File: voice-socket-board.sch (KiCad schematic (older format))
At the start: 290 parts, among them J1 JACK_MONO_SW, J2 JACK_MONO_SW, J3 JACK_MONO_SW, P1 CONN_01X03, P2 CONN_01X03, P3 CONN_02X05, P4 DDR3-DIMM, Q1 MMBT3904, Q10 2N3906, Q2 DMMT3904W, Q3 2N7002, Q4 2N7002, Q5 MMBT3904, Q6 2N3906, Q7 MMBT3904, Q8 MMBT3904, Q9 MMBT3904, SW1 SPST, SW10 SP3T, SW11 SP3T, SW12 SP3T, SW13 SP3T, SW14 SPST, SW15 TACT_SWITCH, SW2 SPST, SW3 SP3T, SW4 SP3T, SW5 SPST, SW6 SPST, SW7 Switch_SPDT_x2, SW8 2P3T, SW9 SP3T, U1 LM833, U10 TL072-, U11 NE5534, U2 TL072-, U3 TL072-, U4 TL072-, U5 TL072-, U6 TL072-, U7 MAX9945, U8 CD4013, U9 TL072-

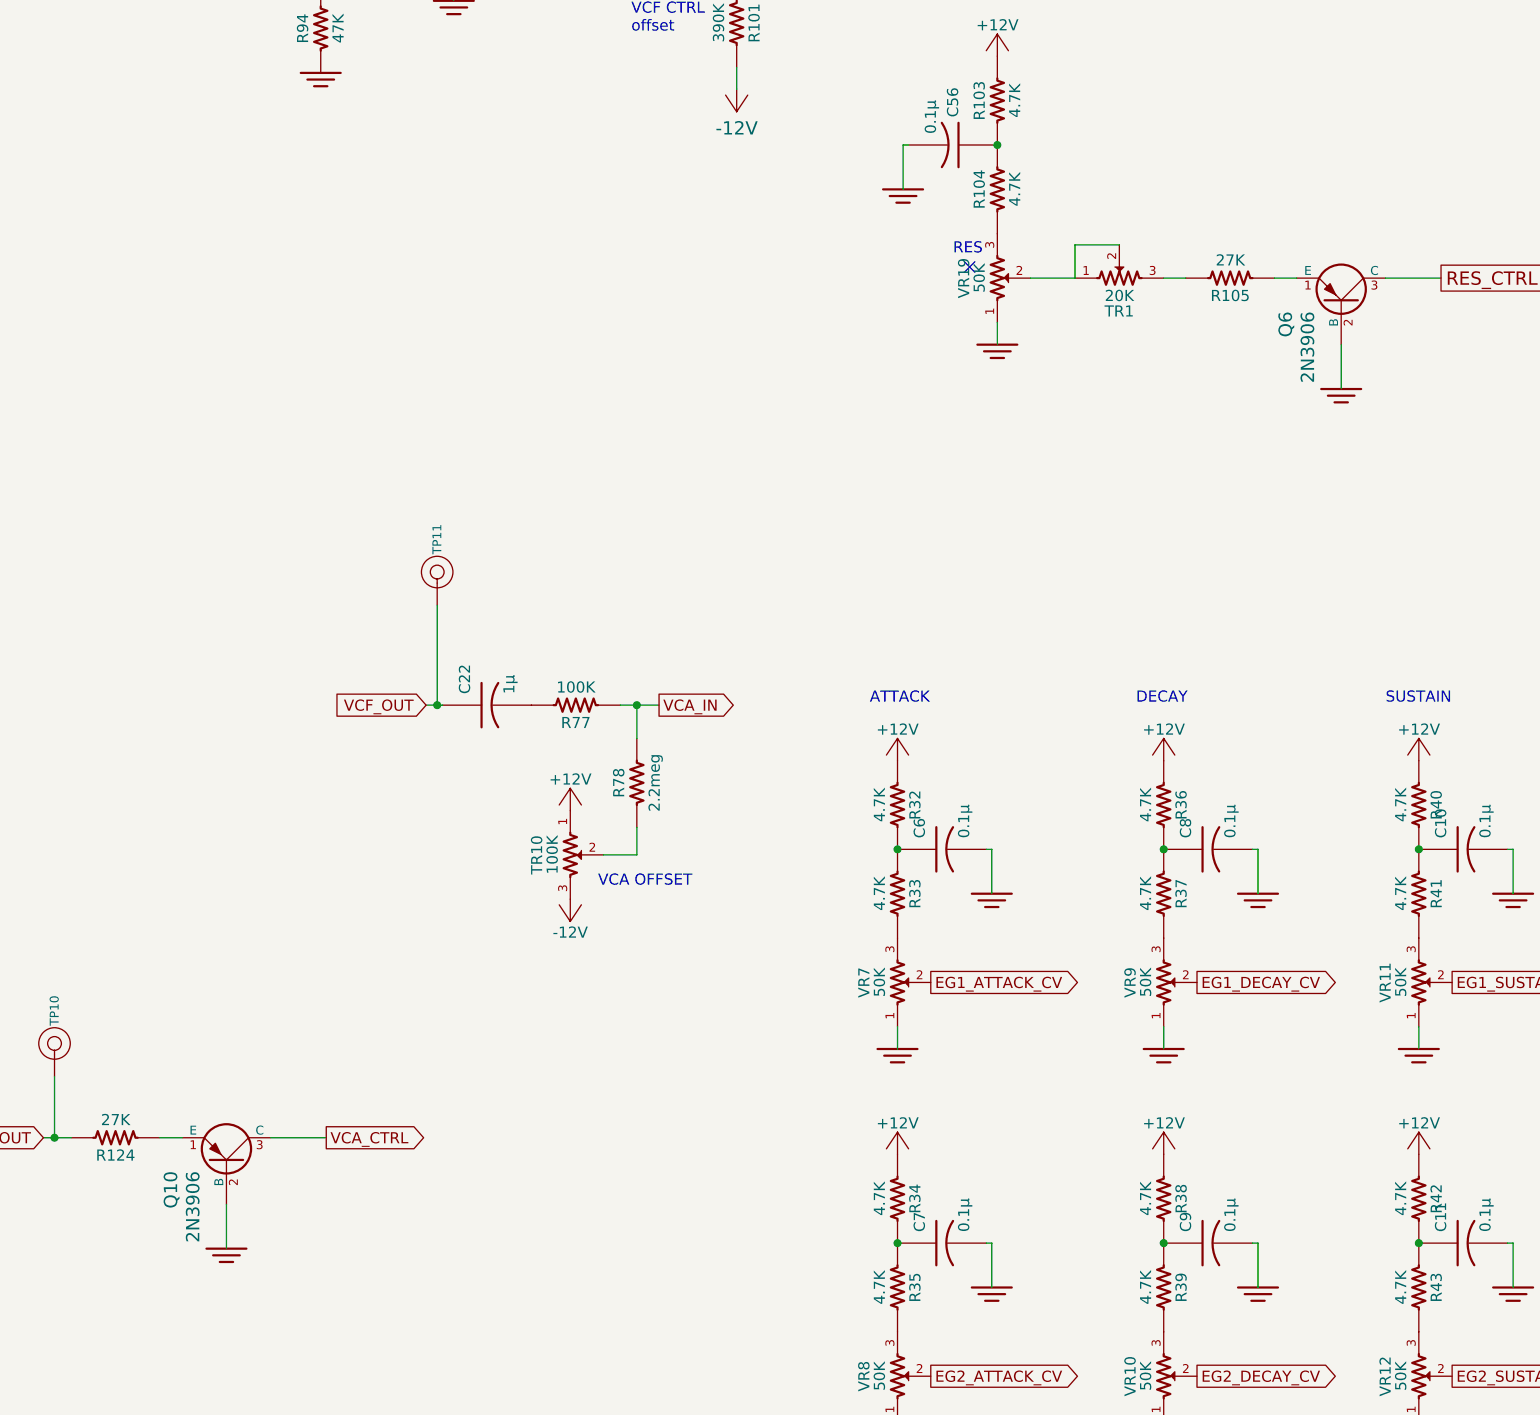
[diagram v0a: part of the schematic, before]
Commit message: changing out all SOT23 footprints for SOT23-132 - pin numbering was previously inconsistent and incoorect for LM4040 and MMBT3904 symbols and footprints
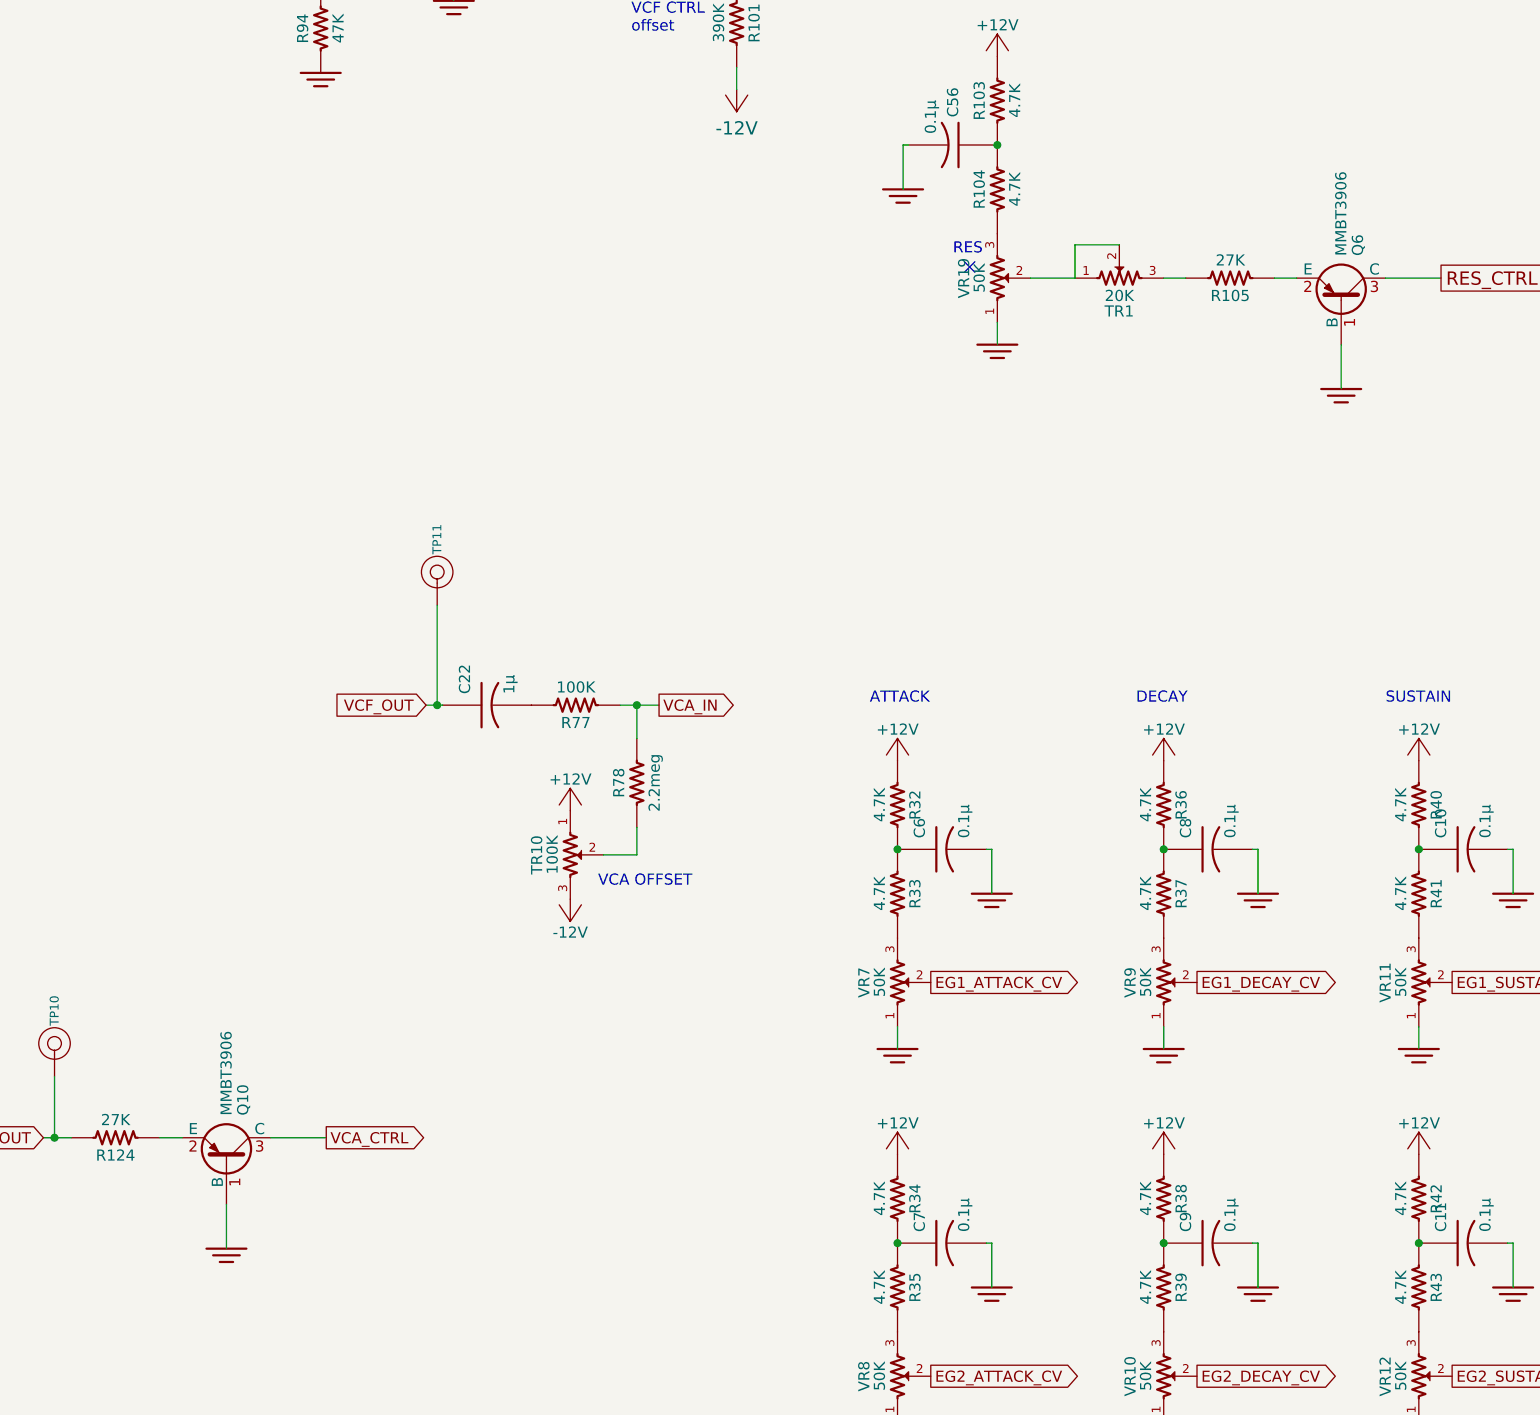
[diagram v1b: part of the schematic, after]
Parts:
- removed Q10, Q6: 2N3906, MyModules:SOT23-JRL, symbol PNP
- added Q10, Q6: MMBT3906, MyModules:SOT23-132-JRL, symbol MMBT3906
- D10, D11: footprint MyModules:SMB -> MyModules:SMB-1C2A
- Q1, Q5, Q7, Q8, Q9: footprint MyModules:SOT23-JRL -> MyModules:SOT23-132-JRL
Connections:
- net GND: now also Q10.1 (B), Q6.1 (B)
- net RES_CTRL: now also Q6.3 (C)
- net VCA_CTRL: now also Q10.3 (C)
- net at R105.1: now also Q6.2 (E)
- net at R124.1: now also Q10.2 (E)
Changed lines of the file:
@@
 $EndComp
 $Comp
-L PNP Q6
-U 1 1 5664F02B
-P 22300 25625
-F 0 "Q6" H 22250 25375 60  0000 R CNN
-F 1 "2N3906" H 22250 25475 60  0000 R CNN
-F 2 "MyModules:SOT23-JRL" H 22300 25625 60  0001 C CNN
-F 3 "~" H 22300 25625 60  0000 C CNN
-	1    22300 25625
-	0    1    -1   0
-$EndComp
-$Comp
 L POT_US TR1
 U 1 1 5664F02C
@@
 F 0 "Q7" H 11200 26125 50  0000 L CNN
 F 1 "MMBT3904" H 11200 26050 50  0000 L CNN
-F 2 "MyModules:SOT23-JRL" H 11200 25975 50  0001 L CIN
+F 2 "MyModules:SOT23-132-JRL" H 11200 25975 50  0001 L CIN
 F 3 "" H 11000 26050 50  0000 L CNN
 	1    11000 26050
@@
 F 0 "Q8" H 11200 27550 50  0000 L CNN
 F 1 "MMBT3904" H 11200 27475 50  0000 L CNN
-F 2 "MyModules:SOT23-JRL" H 11200 27400 50  0001 L CIN
+F 2 "MyModules:SOT23-132-JRL" H 11200 27400 50  0001 L CIN
 F 3 "" H 11000 27475 50  0000 L CNN
 	1    11000 27475
@@
 F 0 "Q9" H 14550 28075 50  0000 L CNN
 F 1 "MMBT3904" H 14550 28000 50  0000 L CNN
-F 2 "MyModules:SOT23-JRL" H 14550 27925 50  0001 L CIN
+F 2 "MyModules:SOT23-132-JRL" H 14550 27925 50  0001 L CIN
 F 3 "" H 14350 28000 50  0000 L CNN
 	1    14350 28000
@@
 F 0 "Q5" H 17375 18625 50  0000 L CNN
 F 1 "MMBT3904" H 17375 18550 50  0000 L CNN
-F 2 "MyModules:SOT23-JRL" H 17375 18475 50  0001 L CIN
+F 2 "MyModules:SOT23-132-JRL" H 17375 18475 50  0001 L CIN
 F 3 "" H 17175 18550 50  0000 L CNN
 	1    17175 18550
@@
 F 0 "Q1" H 16475 12075 50  0000 L CNN
 F 1 "MMBT3904" H 16475 12000 50  0000 L CNN
-F 2 "MyModules:SOT23-JRL" H 16475 11925 50  0001 L CIN
+F 2 "MyModules:SOT23-132-JRL" H 16475 11925 50  0001 L CIN
 F 3 "" H 16275 12000 50  0000 L CNN
 	1    16275 12000
@@
 F 0 "D10" H 40375 1600 50  0000 C CNN
 F 1 "D" H 40375 1400 50  0000 C CNN
-F 2 "MyModules:SMB" H 40375 1500 60  0001 C CNN
+F 2 "MyModules:SMB-1C2A" H 40375 1500 60  0001 C CNN
 F 3 "" H 40375 1500 60  0000 C CNN
 	1    40375 1500
@@
 F 0 "D11" H 40375 2050 50  0000 C CNN
 F 1 "D" H 40375 1850 50  0000 C CNN
-F 2 "MyModules:SMB" H 40375 1950 60  0001 C CNN
+F 2 "MyModules:SMB-1C2A" H 40375 1950 60  0001 C CNN
 F 3 "" H 40375 1950 60  0000 C CNN
 	1    40375 1950
@@
 Connection ~ 9250 28550
 $Comp
-L PNP Q10
-U 1 1 56706FF4
-P 17275 29500
-F 0 "Q10" H 17225 29250 60  0000 R CNN
-F 1 "2N3906" H 17225 29350 60  0000 R CNN
-F 2 "MyModules:SOT23-JRL" H 17275 29500 60  0001 C CNN
-F 3 "~" H 17275 29500 60  0000 C CNN
-	1    17275 29500
-	0    1    -1   0
-$EndComp
-$Comp
 L R_US R124
 U 1 1 56706FFA
@@
 	18175 27450 18250 27450
 Connection ~ 18225 27450
+$Comp
+L MMBT3906 Q6
+U 1 1 5679132E
+P 22300 25625
+F 0 "Q6" H 22500 25700 50  0000 L CNN
+F 1 "MMBT3906" H 22500 25625 50  0000 L CNN
+F 2 "MyModules:SOT23-132-JRL" H 22500 25550 50  0001 L CIN
+F 3 "" H 22300 25625 50  0000 L CNN
+	1    22300 25625
+	0    1    -1   0
+$EndComp
+$Comp
+L MMBT3906 Q10
+U 1 1 5679371D
+P 17275 29500
+F 0 "Q10" H 17475 29575 50  0000 L CNN
+F 1 "MMBT3906" H 17475 29500 50  0000 L CNN
+F 2 "MyModules:SOT23-132-JRL" H 17475 29425 50  0001 L CIN
+F 3 "" H 17275 29500 50  0000 L CNN
+	1    17275 29500
+	0    1    -1   0
+$EndComp
 $EndSCHEMATC

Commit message: SOT23 footprints updated. double check MMBT3906
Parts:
- D1, D2: footprint MyModules:SOT23-JRL -> MyModules:SOT23-132-JRL

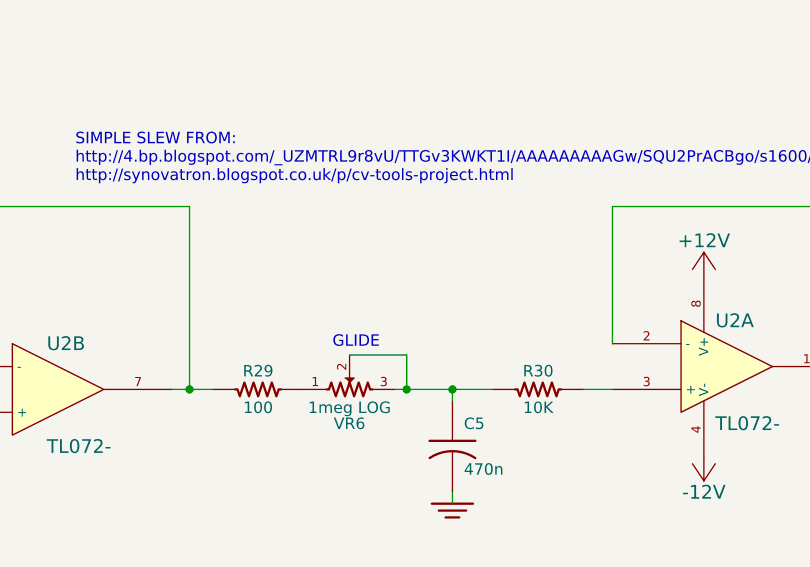
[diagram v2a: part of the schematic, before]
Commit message: adjust silkscreen references. about to add filter freq mod switch
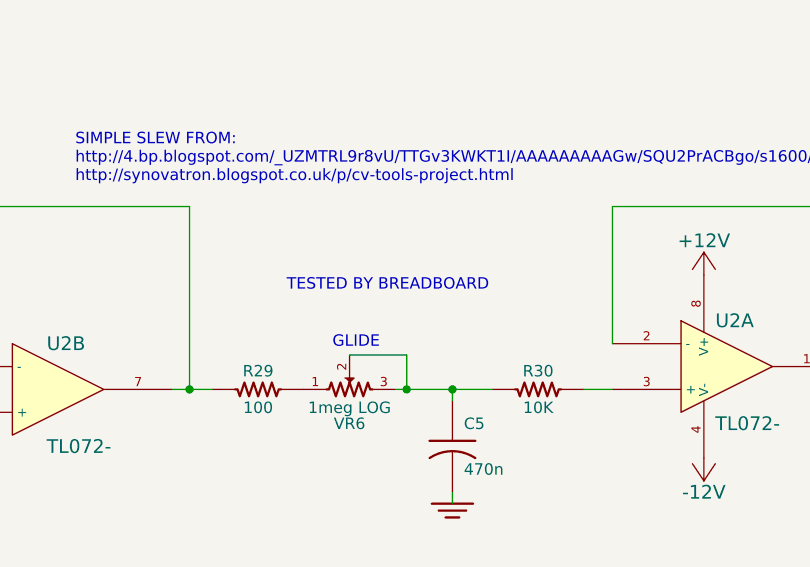
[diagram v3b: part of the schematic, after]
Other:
- note added: "TESTED BY BREADBOARD"
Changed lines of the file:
@@
 	0    1    -1   0
 $EndComp
+Text Notes 30525 9800 0    50   ~ 0
+TESTED BY BREADBOARD
 $EndSCHEMATC

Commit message: added filter FM switch
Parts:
- added C63, C64: 0.1μ, MyModules:SM0603-C-JRL, symbol C_US
- added R125, R126: 47K, MyModules:SM0603-R-JRL, symbol R_US
- added R127: 100K, MyModules:SM0603-R-JRL, symbol R_US
- added SW16: SP3T, MyModules:SS-23E02-2P3T-SLIDE, symbol SP3T
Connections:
- net +12V: now also C63.1
- net -12V: now also C64.2
- net GND: now also C63.2, C64.1, R126.1, SW16.1
- net VCO1_SAW: now also R125.2, SW16.4
- net at C57.1, R100.1, R101.1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: now also R127.1
- new net: R125.1, R126.2, SW16.2
- new net: R127.2, SW16.3
- no-connect marks 12 -> 11
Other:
- note added: "VCF FM\n\n"
- moved on the sheet: R101, VR1, VR2
